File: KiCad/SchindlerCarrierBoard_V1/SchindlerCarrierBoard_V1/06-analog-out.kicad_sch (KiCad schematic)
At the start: 33 parts, among them J600 73101-0120 (CVBS OUT), J601 73101-0120 (component Y OUT), J602 73101-0120 (component Pb OUT), J603 73101-0120 (component Pr OUT), U600 ADV7393BCPZ-REEL, U601 LMH6643MAX/NOPB (out buf A/B), U602 LMH6643MAX/NOPB (out buf A/B)

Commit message: Schindler 2.0: checkpoint — decoupling + functional audit, pre-edit save
Saves current carrier schematic state (all 12 sheets, KiCad re-saves) and
project docs before starting the decoupling/functional-fix wiring pass.

- docs/decoupling-audit.md: full per-chip decoupling audit (EXISTS /
  DATASHEET WANTS / PROPOSED ADDS) + "Functional fixes" section
  (COMP/PWRDWN*/VREG_VOUT floating, Y900 load caps; clocks verified
  present). ~91 proposed caps + ferrites; report-only, nothing placed.
- Other docs (bom-v1, refdes-map, spec, part-lock, etc.) synced.

No wiring changes — proposals await gate. Reference binaries (datasheet
JPGs/PDF, Manufacturing/) intentionally left untracked.

Co-Authored-By: Claude Opus 4.8 (1M context) <noreply@anthropic.com>
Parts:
- C600, C601, C602, C603, C604, C605: footprint (none) -> Capacitor_SMD:C_0805_2012Metric
- R600, R601, R602, R603, R604, R605, R606, R607, R608, R609, R610, R611, R612, R613, R614, R615: footprint (none) -> Resistor_SMD:R_0805_2012Metric
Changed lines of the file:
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@@
 			)
 		)
-		(property "Footprint" ""
+		(property "Footprint" "Capacitor_SMD:C_0805_2012Metric"
 			(at 265.43 219.71 0)
 			(hide yes)
@@
 			)
 		)
-		(property "Footprint" ""
+		(property "Footprint" "Resistor_SMD:R_0805_2012Metric"
 			(at 115.57 160.02 0)
 			(hide yes)
@@
 			)
 		)
-		(property "Footprint" ""
+		(property "Footprint" "Resistor_SMD:R_0805_2012Metric"
 			(at 340.36 160.02 0)
 			(hide yes)
@@
 			)
 		)
-		(property "Footprint" ""
+		(property "Footprint" "Resistor_SMD:R_0805_2012Metric"
 			(at 115.57 100.33 0)
 			(hide yes)
@@
 			)
 		)
-		(property "Footprint" ""
+		(property "Footprint" "Resistor_SMD:R_0805_2012Metric"
 			(at 265.43 100.33 0)
 			(hide yes)
@@
 			)
 		)
-		(property "Footprint" ""
+		(property "Footprint" "Resistor_SMD:R_0805_2012Metric"
 			(at 190.5 100.33 0)
 			(hide yes)
@@
 			)
 		)
-		(property "Footprint" ""
+		(property "Footprint" "Resistor_SMD:R_0805_2012Metric"
 			(at 265.43 160.02 0)
 			(hide yes)
@@
 			)
 		)
-		(property "Footprint" ""
+		(property "Footprint" "Resistor_SMD:R_0805_2012Metric"
 			(at 115.57 219.71 0)
 			(hide yes)
@@
 			)
 		)
-		(property "Footprint" ""
+		(property "Footprint" "Resistor_SMD:R_0805_2012Metric"
 			(at 39.37 160.02 0)
 			(hide yes)
@@
 			)
 		)
-		(property "Footprint" ""
+		(property "Footprint" "Resistor_SMD:R_0805_2012Metric"
 			(at 39.37 100.33 0)
 			(hide yes)
@@
 			)
 		)
-		(property "Footprint" ""
+		(property "Footprint" "Resistor_SMD:R_0805_2012Metric"
 			(at 415.29 100.33 0)
 			(hide yes)
@@
 			)
 		)
-		(property "Footprint" ""
+		(property "Footprint" "Resistor_SMD:R_0805_2012Metric"
 			(at 39.37 219.71 0)
 			(hide yes)
@@
 			)
 		)
-		(property "Footprint" ""
+		(property "Footprint" "Resistor_SMD:R_0805_2012Metric"
 			(at 490.22 100.33 0)
 			(hide yes)
@@
 			)
 		)
-		(property "Footprint" ""
+		(property "Footprint" "Capacitor_SMD:C_0805_2012Metric"
 			(at 190.5 219.71 0)
 			(hide yes)
@@
 			)
 		)
-		(property "Footprint" ""
+		(property "Footprint" "Resistor_SMD:R_0805_2012Metric"
 			(at 490.22 160.02 0)
 			(hide yes)
@@
 			)
 		)
-		(property "Footprint" ""
+		(property "Footprint" "Resistor_SMD:R_0805_2012Metric"
 			(at 415.29 160.02 0)
 			(hide yes)
@@
 			)
 		)
-		(property "Footprint" ""
+		(property "Footprint" "Capacitor_SMD:C_0805_2012Metric"
 			(at 415.29 219.71 0)
 			(hide yes)
@@
 			)
 		)
-		(property "Footprint" ""
+		(property "Footprint" "Resistor_SMD:R_0805_2012Metric"
 			(at 190.5 160.02 0)
 			(hide yes)
@@
 			)
 		)
-		(property "Footprint" ""
+		(property "Footprint" "Capacitor_SMD:C_0805_2012Metric"
 			(at 490.22 219.71 0)
 			(hide yes)
@@
 			)
 		)
-		(property "Footprint" ""
+		(property "Footprint" "Capacitor_SMD:C_0805_2012Metric"
 			(at 340.36 219.71 0)
 			(hide yes)
@@
 			)
 		)
-		(property "Footprint" ""
+		(property "Footprint" "Resistor_SMD:R_0805_2012Metric"
 			(at 340.36 100.33 0)
 			(hide yes)
@@
 			)
 		)
-		(property "Footprint" ""
+		(property "Footprint" "Capacitor_SMD:C_0805_2012Metric"
 			(at 39.37 279.4 0)
 			(hide yes)

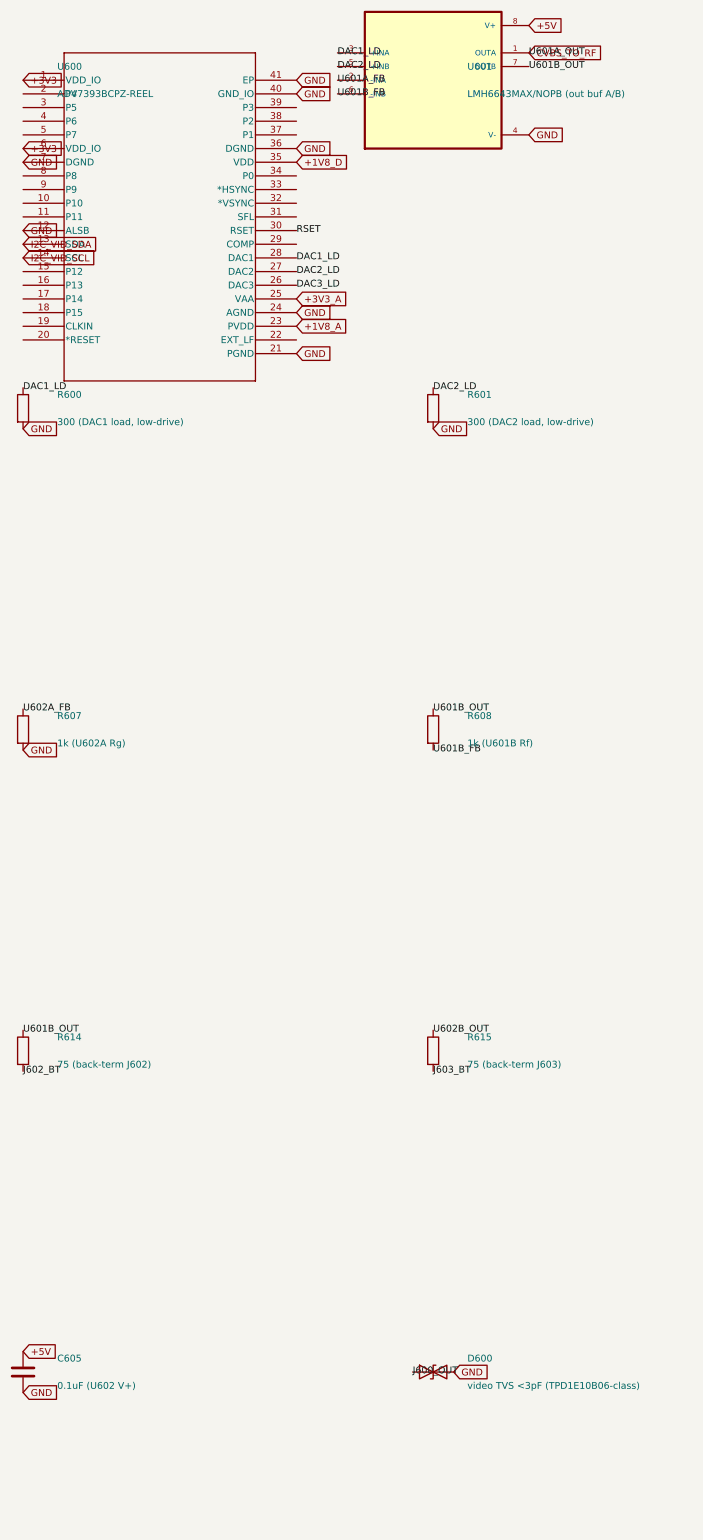
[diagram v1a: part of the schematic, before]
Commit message: Schindler carrier: ADV7511 R_EXT/AVDD fix + symbol relabel; 116 PL nets wired; connector/riser decisions
- U403 ADV7511: add R406 (887R 1%) pin28 R_EXT->GND; wire pin29 AVDD->+1V8_A (match 34/41).
  Sheet-4 ERC pin_not_connected 2->0. Fixes missing TMDS bias ref + unpowered AVDD
  (would-not-work HDMI-out bug, caught pre-fab).
- JustinLibrary ADV7511KSTZ symbol relabel: pin2 SYNC->VSYNC, 28 EXT->R_EXT, 29 R_EXT->AVDD
  (cosmetic; connectivity is by pin number). [NOTE: JustinLibrary is unversioned/external — not in this repo; see report.]
- Pin-lock: 116 PL nets wired; ERC unconnected 899->668; schindler_plio.xdc + pin-lock-assignment.md.
- Connector domain + analog I/O riser decided (connector-domain.md); riser-mezzanine-plan.md rev2
  (gated proposal, not implemented).
- bom-v1 (R406), refdes-map (R406 + symbol-mislabel note), changelog.

Deferred to next commit (kept out so this push stays honest): eeschema Update Symbols from
Library on U403 (display refresh); netlist regen; HDMI +5V power_pin_not_driven x2 (J400/J401.18)
verification; riser stays gated.

Co-Authored-By: Claude Opus 4.8 (1M context) <noreply@anthropic.com>
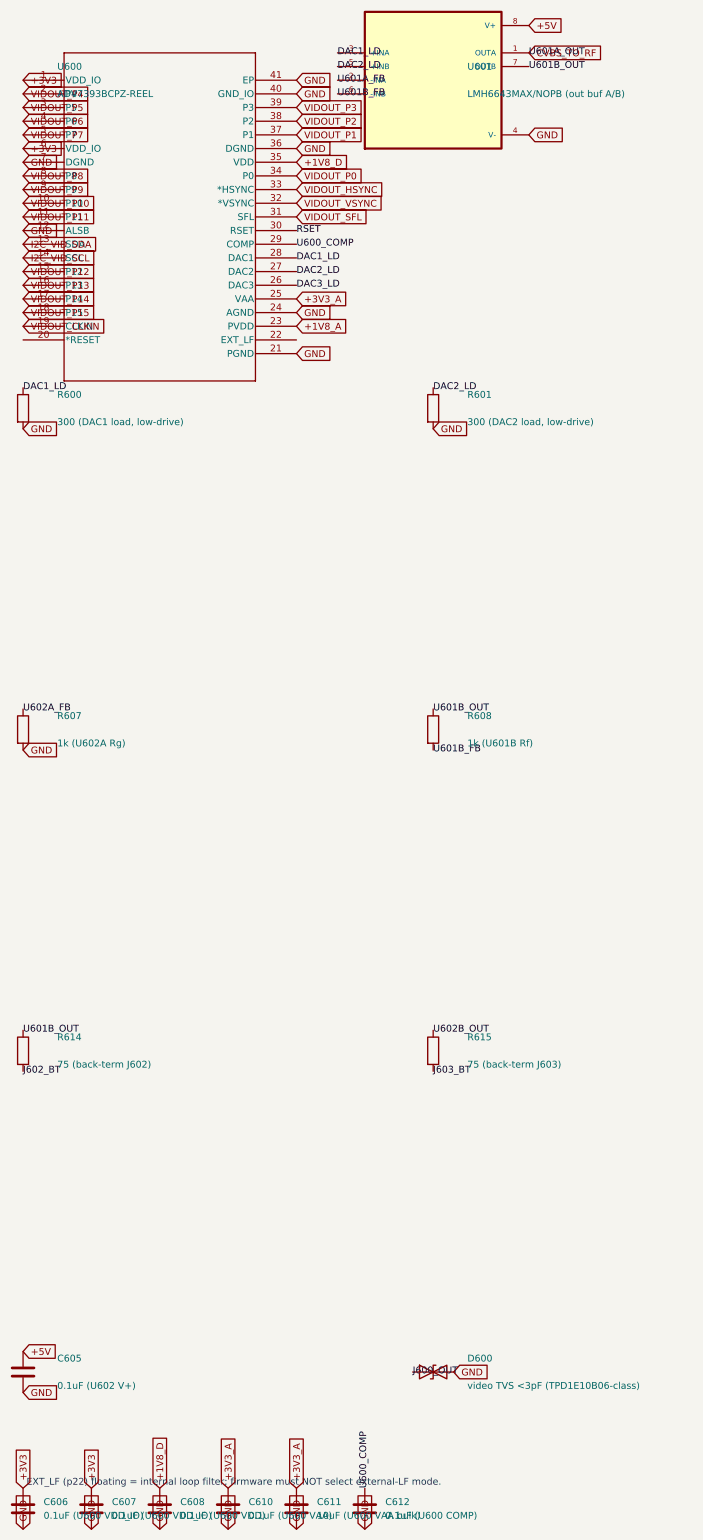
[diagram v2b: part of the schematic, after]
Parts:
- added C606, C607: 0.1uF (U600 VDD_IO), Capacitor_SMD:C_0805_2012Metric, symbol Device:C
- added C608: 0.1uF (U600 VDD), Capacitor_SMD:C_0805_2012Metric, symbol Device:C
- added C610: 0.1uF (U600 VAA), Capacitor_SMD:C_0805_2012Metric, symbol Device:C
- added C611: 10uF (U600 VAA bulk), Capacitor_SMD:C_0805_2012Metric, symbol Device:C
- added C612: 0.1uF (U600 COMP), Capacitor_SMD:C_0805_2012Metric, symbol Device:C
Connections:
- net +1V8_D: now also C608.1
- net +3V3: now also C606.1, C607.1
- net +3V3_A: now also C610.1, C611.1
- net GND: now also C606.2, C607.2, C608.2, C610.2, C611.2, C612.2
- net VIDOUT_P10: now reaches U600.10 (P10)
- net VIDOUT_P11: now reaches U600.11 (P11)
- net VIDOUT_P12: now reaches U600.15 (P12)
- net VIDOUT_P13: now reaches U600.16 (P13)
- net VIDOUT_P14: now reaches U600.17 (P14)
- net VIDOUT_P15: now reaches U600.18 (P15)
- net VIDOUT_CLKIN: now reaches U600.19 (CLKIN)
- net VIDOUT_P4: now reaches U600.2 (P4)
- net U600_COMP: now reaches U600.29 (COMP)
- net U600_COMP: now also C612.1
- net VIDOUT_P5: now reaches U600.3 (P5)
- net VIDOUT_SFL: now reaches U600.31 (SFL)
- net VIDOUT_VSYNC: now reaches U600.32 (*VSYNC)
- net VIDOUT_HSYNC: now reaches U600.33 (*HSYNC)
- net VIDOUT_P0: now reaches U600.34 (P0)
- net VIDOUT_P1: now reaches U600.37 (P1)
- net VIDOUT_P2: now reaches U600.38 (P2)
- net VIDOUT_P3: now reaches U600.39 (P3)
- net VIDOUT_P6: now reaches U600.4 (P6)
- net VIDOUT_P7: now reaches U600.5 (P7)
- net VIDOUT_P8: now reaches U600.8 (P8)
- net VIDOUT_P9: now reaches U600.9 (P9)
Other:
- note added: "EXT_LF (p22) floating = internal loop filter; firmware must NOT select external-LF mode."
